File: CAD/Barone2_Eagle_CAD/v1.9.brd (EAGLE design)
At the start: 101.6 x 101.6 mm, 80 parts, among them J1 USB_C_Port_Raspberry_Pi, J2 XT60-M, M1 PIC32MX340F512H-80I/MR, Q1 BSS138, Q2 BSS138, X1 CB3LV-3C-8M0000, Y1 ABRACON_ASEK-32_768KHZ-LRTABR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

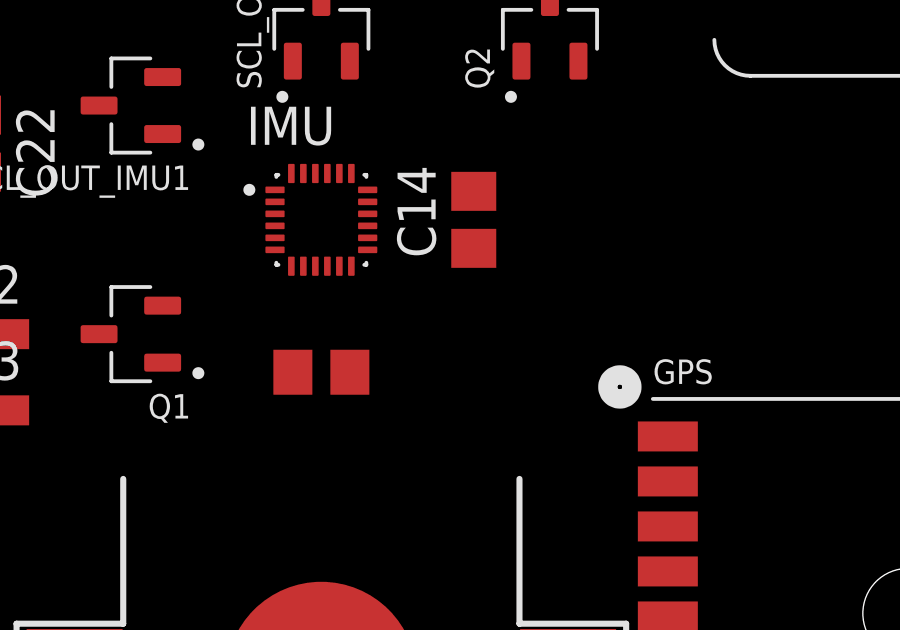
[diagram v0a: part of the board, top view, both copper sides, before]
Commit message: added logic level converter for interupt pin of IMU
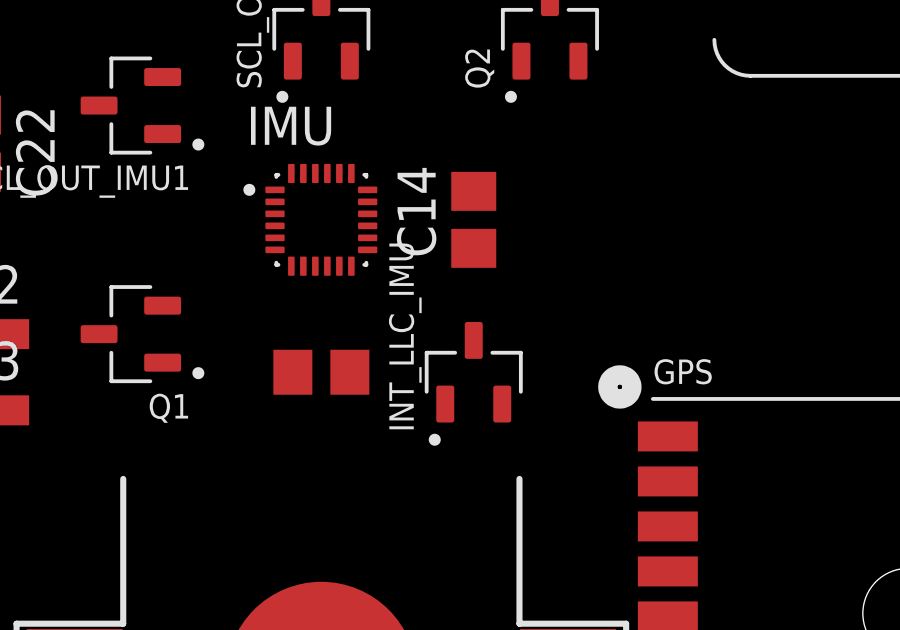
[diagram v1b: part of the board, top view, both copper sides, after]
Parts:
- added INT_LLC_IMU: BSS138, BSS138:SOT95P240X111-3N
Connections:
- new net INT_SOURCE_IMU: IMU.12, INT_LLC_IMU.1
- net INT_IMU: now also INT_LLC_IMU.3; no longer IMU.12
- net VIN: now also INT_LLC_IMU.2
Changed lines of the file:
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@@
 <attribute name="VALUE" x="21.59" y="24.13" size="1.27" layer="27"/>
+</element>
+<element name="INT_LLC_IMU" library="BSS138" package="SOT95P240X111-3N" value="BSS138" x="77.47" y="30.48" smashed="yes" rot="R90">
+<attribute name="AVAILABILITY" value="Good" x="69.85" y="22.86" size="1.778" layer="27" rot="R90" display="off"/>
+<attribute name="DESCRIPTION" value=" N-Channel 50V 220mA (Ta) 360mW (Ta) Surface Mount SOT-23-3 " x="69.85" y="22.86" size="1.778" layer="27" rot="R90" display="off"/>
+<attribute name="MF" value="ON Semiconductor" x="69.85" y="22.86" size="1.778" layer="27" rot="R90" display="off"/>
+<attribute name="MP" value="BSS138" x="69.85" y="22.86" size="1.778" layer="27" rot="R90" display="off"/>
+<attribute name="NAME" x="75.47" y="28.48" size="0.8128" layer="25" rot="R90"/>
+<attribute name="PACKAGE" value="SOT-23 ON" x="69.85" y="22.86" size="1.778" layer="27" rot="R90" display="off"/>
+<attribute name="PRICE" value="None" x="69.85" y="22.86" size="1.778" layer="27" rot="R90" display="off"/>
+<attribute name="PURCHASE-URL" value="https://pricing.snapeda.com/search/part/BSS138/?ref=eda" x="69.85" y="22.86" size="1.778" layer="27" rot="R90" display="off"/>
+<attribute name="VALUE" x="79.47" y="28.48" size="0.8128" layer="27" rot="R90" align="top-left"/>
 </element>
 </elements>
@@
 <contactref element="C29" pad="1"/>
 <contactref element="5V_SRVO_2" pad="3"/>
+<contactref element="INT_LLC_IMU" pad="2"/>
 <wire x1="90.66" y1="91.18" x2="92.39" y2="96.52" width="0" layer="19" extent="1-1"/>
 <wire x1="73.03" y1="91.73" x2="90.66" y2="91.18" width="0" layer="19" extent="1-1"/>
@@
 <wire x1="27.13" y1="83.53" x2="27.43" y2="91.73" width="0" layer="19" extent="1-1"/>
 <wire x1="22.93" y1="83.53" x2="27.13" y2="83.53" width="0" layer="19" extent="1-1"/>
+<wire x1="78.42" y1="29.42" x2="9.21" y2="26.67" width="0" layer="19" extent="1-1"/>
 </signal>
 <signal name="ECHO_SON0">
@@
 </signal>
 <signal name="INT_IMU">
-<contactref element="IMU" pad="12"/>
 <contactref element="M1" pad="5"/>
-<wire x1="42.605" y1="37.31" x2="73.39" y2="34.015" width="0" layer="19" extent="1-1"/>
+<contactref element="INT_LLC_IMU" pad="3"/>
+<wire x1="77.47" y1="31.54" x2="42.605" y2="37.31" width="0" layer="19" extent="1-1"/>
 </signal>
 <signal name="SCK_M2">
@@
 <wire x1="67.1" y1="32.7" x2="71.79" y2="34.015" width="0" layer="19" extent="1-1"/>
 </signal>
+<signal name="INT_SOURCE_IMU">
+<contactref element="IMU" pad="12"/>
+<contactref element="INT_LLC_IMU" pad="1"/>
+<wire x1="76.52" y1="29.42" x2="73.39" y2="34.015" width="0" layer="19" extent="1-1"/>
+</signal>
 </signals>

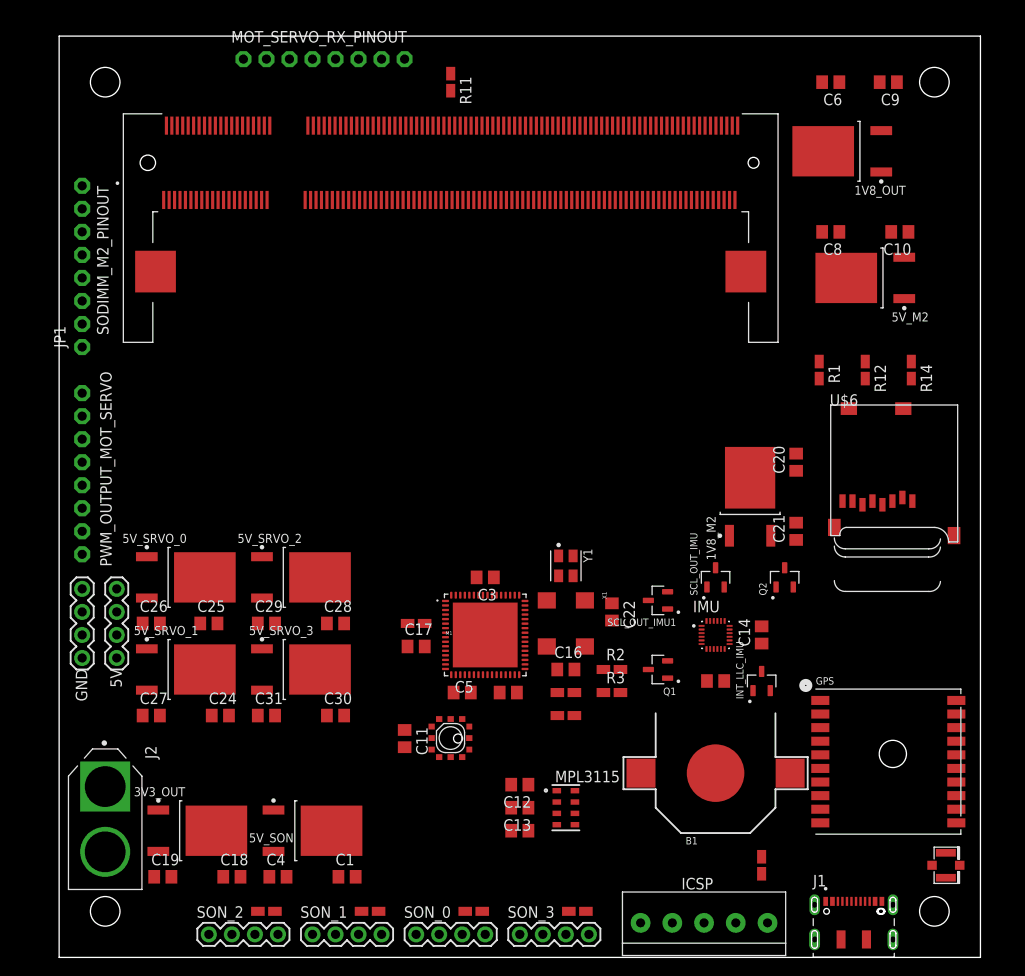
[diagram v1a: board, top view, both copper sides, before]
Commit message: Added Transmitter pinout
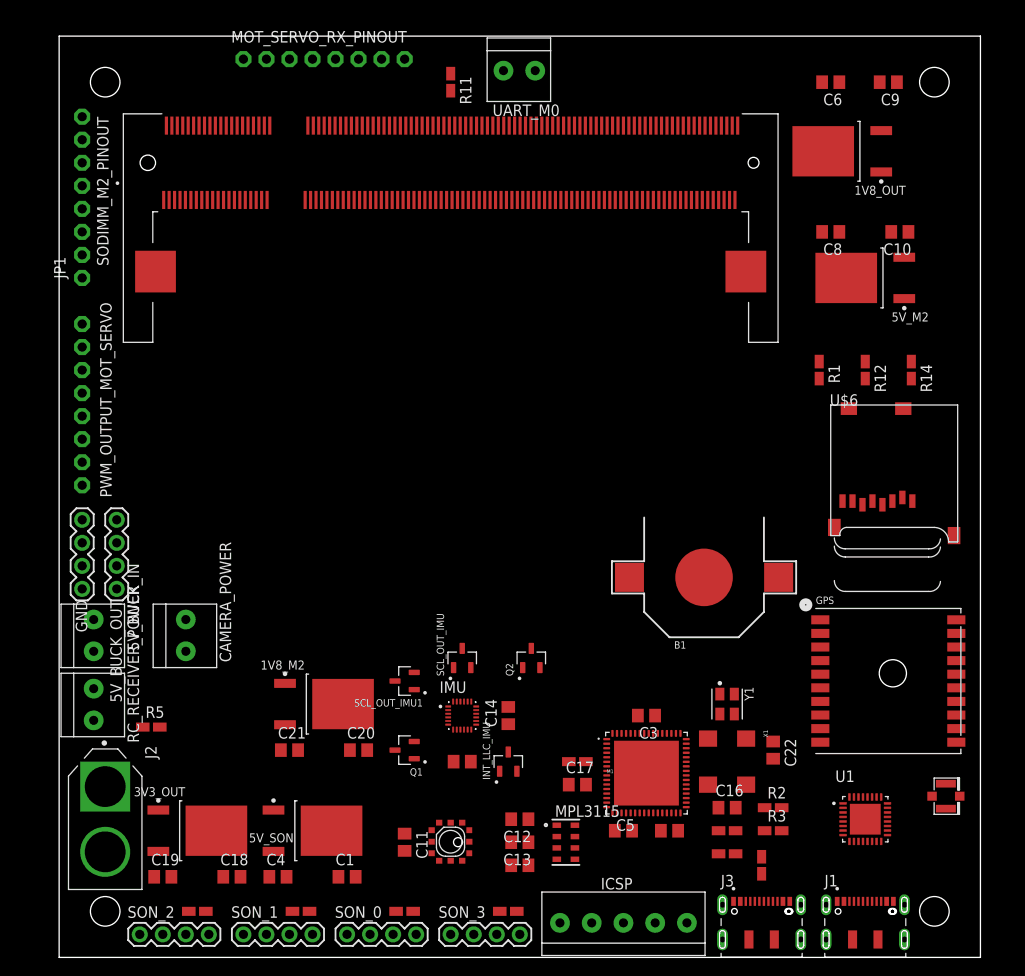
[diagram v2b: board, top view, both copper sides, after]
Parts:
- removed 5V: 1X4-BIG, adafruit:1X04-BIG
- removed 5V_SRVO_0, 5V_SRVO_1, 5V_SRVO_2, 5V_SRVO_3: STMICROELECTRONICS_LD1117DT33CTRSTMICROELECTRONICS_LD1117DT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, STMicroelectronics - LD1117DT33CTR:STMICROELECTRONICS_LD1117DT33CTR_2
- removed C24, C25, C28, C30: 10uF, rcl:C0805
- removed C26, C27, C29, C31: 0.1uF, rcl:C0805
- added 5V_BUCK_IN, CAMERA_POWER, RC_RECEIVER_POWER, UART_M0: 1X2-3.5MM, adafruit:1X2-3.5MM
- added 5V_BUCK_OUT: 1X4-BIG, adafruit:1X04-BIG
- added J3: USB_C_Port_PIC32, DX07S016JA1R1500:JAE_DX07S016JA1R1500
- added R5: 47k, adafruit:R0805W
- added U1: FT232RQ, FT232RQ:QFN50P500X500X90-33N
- moved C21 60.9 mm to (25.4, 22.9), turned to 0 degrees
- moved C20 57.8 mm to (33.0, 22.9), turned to 0 degrees
- moved 1V8_M2 52.3 mm to (29.2, 27.9), turned to 0 degrees
- moved Q1 29.3 mm to (38.1, 22.9)
- moved Q2 29.3 mm to (52.1, 33.0)
- moved SCL_OUT_IMU1 29.3 mm to (38.1, 30.5)
- moved C14 29.3 mm to (49.5, 26.7)
- moved C2 29.3 mm to (44.5, 21.6)
- moved IMU 29.3 mm to (44.5, 26.7)
- moved INT_LLC_IMU 29.3 mm to (49.5, 21.6)
- moved SCL_OUT_IMU 29.3 mm to (44.5, 33.0)
- moved C15 23.4 mm to (67.3, 14.0)
- moved C17 23.4 mm to (57.1, 19.1)
- moved R15 23.4 mm to (57.1, 21.6)
- moved C22 23.4 mm to (78.7, 22.9)
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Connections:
- removed net 5V1: 5V.1, 5V_SRVO_3.4, C30.1
- new net N$14: R5.2, RC_RECEIVER_POWER.1
- new net RXD0_M2: SODIMM_M2_PINOUT.60, UART_M0.2
- new net TXD0_M2: SODIMM_M2_PINOUT.58, UART_M0.1
- new net U2RX_M1: M1.31, U1.30
- new net U2TX_M1: M1.32, U1.2
- net 5V: now also U1.19; no longer 5V.4, 5V_SRVO_0.4, C25.1
- net 9.6V-12.6V: now also CAMERA_POWER.1, R5.1
- net EXP: now also U1.33
- net GND: now also 5V_BUCK_IN.2, CAMERA_POWER.2, J3.1, J3.12, J3.S1, J3.S2, J3.S3, J3.S4, J3.S5, J3.S6, RC_RECEIVER_POWER.2, U1.17, U1.20, U1.24, U1.26, U1.4; no longer 5V_SRVO_0.1, 5V_SRVO_1.1, 5V_SRVO_2.1, 5V_SRVO_3.1, C24.2, C25.2, C26.2, C27.2, C28.2, C29.2, C30.2, C31.2
- net N$12: no longer 5V_SRVO_0.3, C26.1
- net N$15: now also J3.5, J3.8, U1.15; no longer 5V.2, 5V_SRVO_2.4, C28.1
- net N$16: now also J3.6, J3.7, U1.14; no longer 5V_SRVO_3.3, C31.1
- net N$5: now also 5V_BUCK_IN.1, 5V_BUCK_OUT.1, 5V_BUCK_OUT.2, 5V_BUCK_OUT.3, 5V_BUCK_OUT.4; no longer 5V.3, 5V_SRVO_1.4, C24.1
- net VBUS: now also J3.11, J3.2
- net VIN: now also U1.1; no longer 5V_SRVO_1.3, 5V_SRVO_2.3, C27.1, C29.1

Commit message: Fixing ECE121 source code
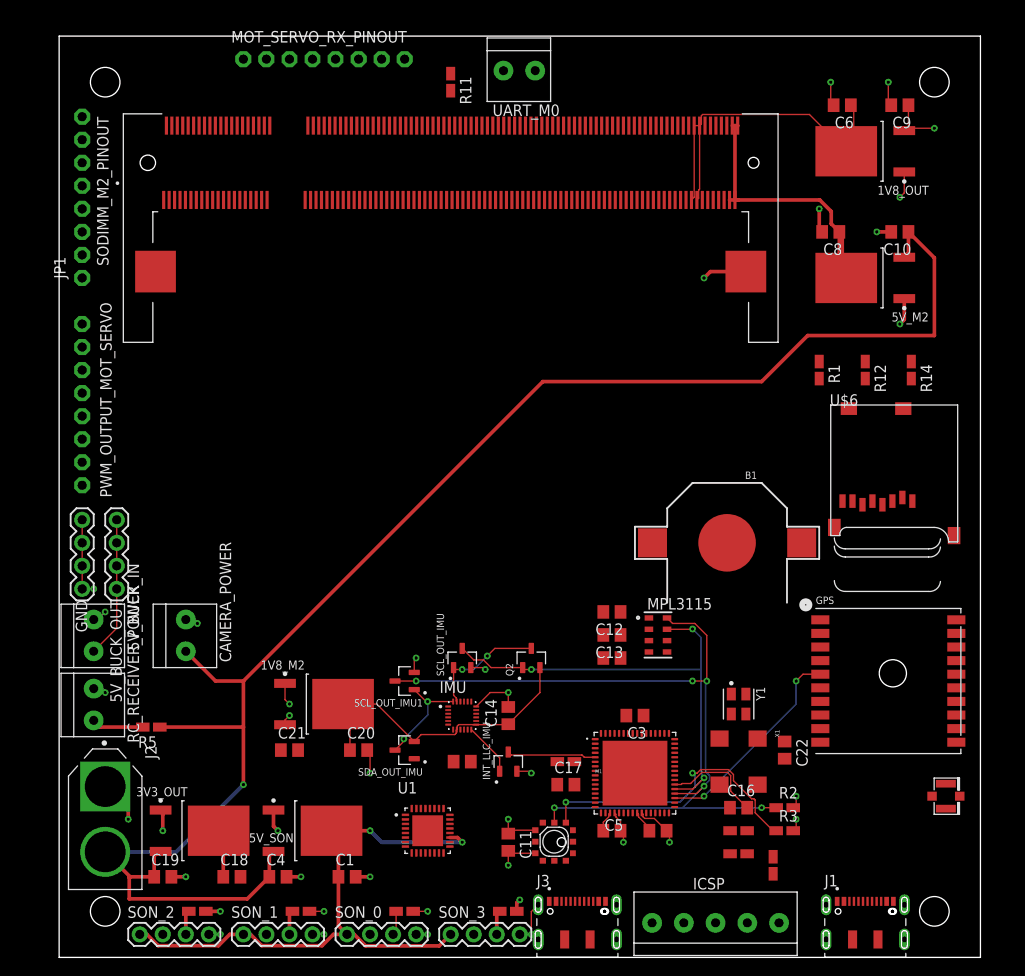
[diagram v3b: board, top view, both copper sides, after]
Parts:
- moved U1 48.3 mm to (40.6, 14.0)
- moved C13 25.0 mm to (61.0, 35.6)
- moved C7 25.0 mm to (61.0, 33.0)
- moved MPL3115 25.0 mm to (66.0, 35.6)
- moved C12 25.0 mm to (61.0, 38.1)
- moved J3 20.3 mm to (57.1, 5.08)
- moved C11 11.4 mm to (49.5, 12.7)
- moved MPR 11.4 mm to (54.6, 12.7)
- moved ICSP 10.2 mm to (72.4, 3.81)
- moved B1 4.58 mm to (73.7, 45.7), turned to 180 degrees
- moved C6 2.84 mm to (86.4, 94.0)
- moved C9 2.84 mm to (92.7, 94.0)
- moved 1V8_OUT 2.54 mm to (88.9, 88.9)
- moved C16 1.27 mm to (74.9, 16.5)
- moved C22 1.27 mm to (80.0, 22.9)
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- renumbered Q1 to SDA_OUT_IMU
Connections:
- removed net CSN_IMU: 1V8_OUT.4, C14.1, C6.1, IMU.13, IMU.22, IMU.8, Q2.2, SDA_OUT_IMU.2
- removed net N$11: 5V_SON.3, C4.1
- removed net N$12: 5V_M2.3, C10.1
- net 1.8V: now also 1V8_OUT.4, C14.1, C6.1, IMU.13, IMU.22, IMU.8, Q2.2, SDA_OUT_IMU.2
- net 9.6V-12.6V: now also 5V_M2.3, 5V_SON.3, C10.1, C4.1
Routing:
- net 9.6V-12.6V: track 0.00 -> 186.5 mm, vias 0 -> 2
- net 5V: track 0.00 -> 97.7 mm, vias 0 -> 2
- net SDA_M1: track 0.00 -> 89.7 mm, vias 0 -> 6
- net SCL_M1: track 0.00 -> 84.5 mm, vias 0 -> 5
- net GND: track 0.00 -> 79.6 mm, vias 0 -> 29
- net 1.8V: track 0.00 -> 71.6 mm
- net GPS_3DFIX: track 0.00 -> 23.2 mm, vias 0 -> 2
- net VIN: track 0.00 -> 20.2 mm, vias 0 -> 8
- net N$5: track 0.00 -> 15.6 mm
- net IMU_SCL: track 0.00 -> 13.4 mm, vias 0 -> 2
- net IMU_SDA: track 0.00 -> 11.7 mm, vias 0 -> 2
- net AVDD3_M1: track 0.00 -> 11.2 mm
- net INT_IMU: track 0.00 -> 9.83 mm
- net INT_SOURCE_IMU: track 0.00 -> 5.89 mm
- net N$14: track 0.00 -> 5.72 mm
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
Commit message: 60% complete with board wiring
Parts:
- removed J1: USB_C_Port_Raspberry_Pi, DX07S016JA1R1500:JAE_DX07S016JA1R1500
- removed J3: USB_C_Port_PIC32, DX07S016JA1R1500:JAE_DX07S016JA1R1500
- added PIC32_USB, RASPBERRY_PI_USB: DX07S016JA1R1500, DX07S016JA1R1500:JAE_DX07S016JA1R1500
- moved R11 59.9 mm to (94.0, 64.8)
- moved R14 5.08 mm to (99.1, 64.8)
- moved C17 3.81 mm to (52.1, 19.1)
- moved R15 3.81 mm to (52.1, 21.6)
- moved C2 1.27 mm to (43.2, 21.6)
- moved INT_LLC_IMU 1.27 mm to (48.3, 21.6)
- moved C15 1.27 mm to (66.0, 12.7)
- moved C5 1.27 mm to (61.0, 12.7)
- moved C3 1.27 mm to (63.5, 27.9)
- turned Y1 to 0 degrees
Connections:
- removed net N$4: R7.2
- net CS_M1: no longer SODIMM_M2_PINOUT.4
- net GND: now also PIC32_USB.1, PIC32_USB.12, PIC32_USB.S1, PIC32_USB.S2, PIC32_USB.S3, PIC32_USB.S4, PIC32_USB.S5, PIC32_USB.S6, RASPBERRY_PI_USB.1, RASPBERRY_PI_USB.12, RASPBERRY_PI_USB.S1, RASPBERRY_PI_USB.S2, RASPBERRY_PI_USB.S3, RASPBERRY_PI_USB.S4, RASPBERRY_PI_USB.S5, RASPBERRY_PI_USB.S6; no longer J1.1, J1.12, J1.S1, J1.S2, J1.S3, J1.S4, J1.S5, J1.S6, J3.1, J3.12, J3.S1, J3.S2, J3.S3, J3.S4, J3.S5, J3.S6
- net N$15: now also PIC32_USB.5, PIC32_USB.8; no longer J3.5, J3.8
- net N$16: now also PIC32_USB.6, PIC32_USB.7; no longer J3.6, J3.7
- net USB_D+_M2: now also RASPBERRY_PI_USB.6, RASPBERRY_PI_USB.7; no longer J1.6, J1.7
- net USB_D-_M2: now also RASPBERRY_PI_USB.5, RASPBERRY_PI_USB.8; no longer J1.5, J1.8
- net VBUS: now also PIC32_USB.11, PIC32_USB.2, RASPBERRY_PI_USB.11, RASPBERRY_PI_USB.2; no longer J1.11, J1.2, J3.11, J3.2
- net VIN: now also R7.2
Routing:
- net GND: track 79.6 -> 299.8 mm, vias 29 -> 58
- net MOSI_M2: track 0.00 -> 159.9 mm, vias 0 -> 5
- net SCK_M2: track 0.00 -> 152.2 mm, vias 0 -> 5
- net MISO_M2: track 0.00 -> 149.8 mm, vias 0 -> 3
- net CS_MICRO_SD: track 0.00 -> 134.3 mm, vias 0 -> 2
- net CS_M1: track 0.00 -> 86.8 mm, vias 0 -> 2
- net TRIG_SON2: track 0.00 -> 65.9 mm, vias 0 -> 1
- net INT1_MPL3115: track 0.00 -> 58.9 mm, vias 0 -> 2
- net TRIG_SON1: track 0.00 -> 56.8 mm, vias 0 -> 1
- net MCLR_M1: track 0.00 -> 47.5 mm
- net TRIG_SON0: track 0.00 -> 42.5 mm, vias 0 -> 1
- net GPIO20_M2: track 0.00 -> 37.1 mm
- net VIN: track 20.2 -> 55.8 mm, vias 8 -> 20
- net GPIO14_M2: track 0.00 -> 34.8 mm, vias 0 -> 1
- net GPIO19_M2: track 0.00 -> 34.8 mm
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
